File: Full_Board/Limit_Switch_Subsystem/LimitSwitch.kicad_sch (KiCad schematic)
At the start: 6 parts, among them J8 OQ0212500000G

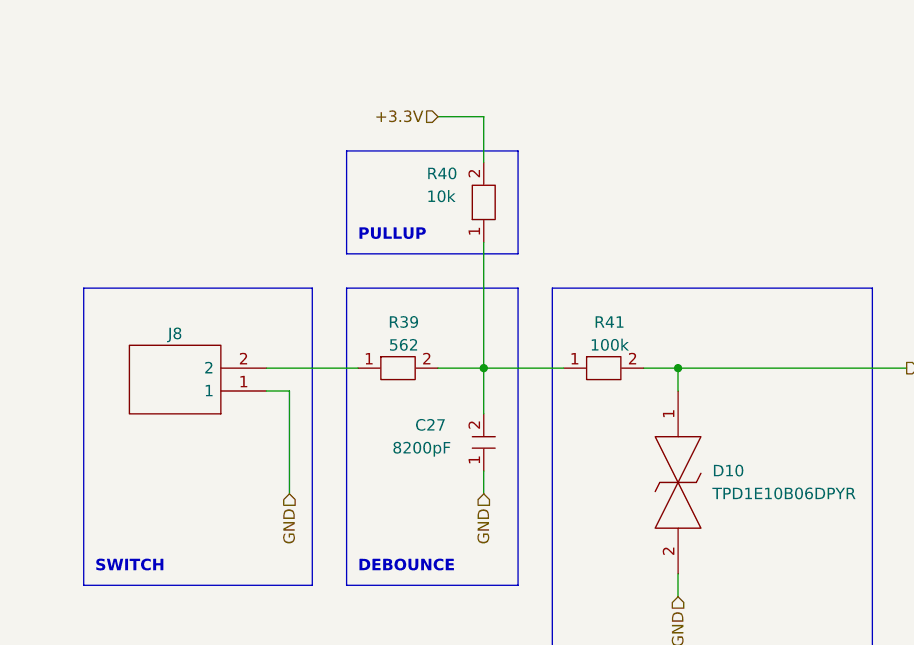
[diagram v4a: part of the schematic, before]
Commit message: Added a fuse and fixed ERC
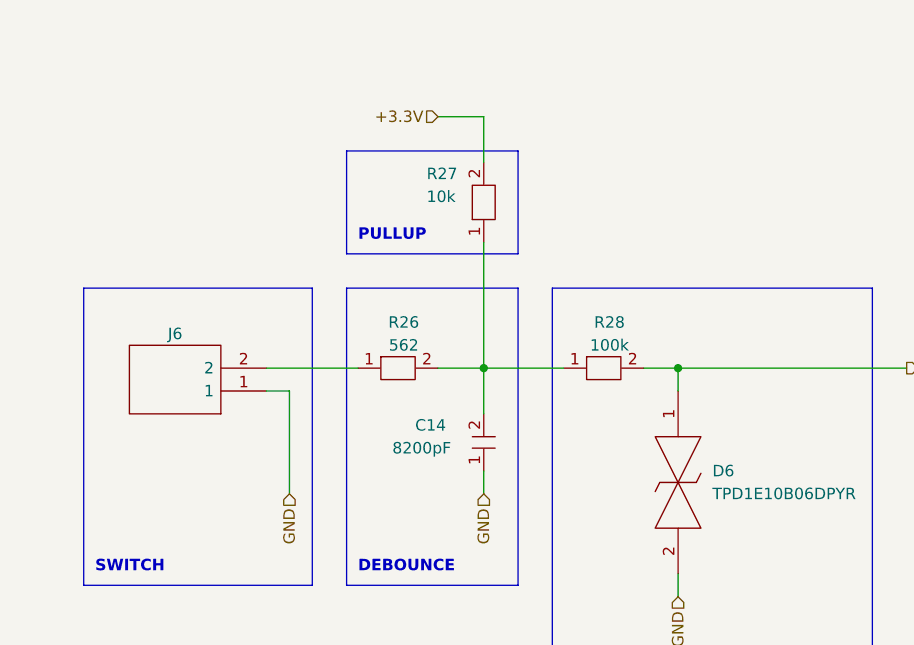
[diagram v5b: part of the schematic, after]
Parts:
- renumbered C27 to C14, D10 to D6, J8 to J6, R39 to R26, R40 to R27, R41 to R28
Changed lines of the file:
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@@
+    (stroke (width 0) (type default) (color 0 0 0 0))
+  )
+  (wire (pts (xy 143.51 62.23) (xy 143.51 67.31))
     (stroke (width 0) (type default) (color 0 0 0 0))
   )
   (wire (pts (xy 165.1 90.17) (xy 190.5 90.17))
-    (stroke (width 0) (type default) (color 0 0 0 0))
-  )
-  (wire (pts (xy 143.51 62.23) (xy 143.51 67.31))
     (stroke (width 0) (type default) (color 0 0 0 0))
   )
@@
     (effects (font (size 1.27 1.27)) (justify right))
   )
-  (symbol (lib_id "OQ0212500000G:OQ0212500000G") (at 119.38 92.71 180) (unit 1)
-    (in_bom yes) (on_board yes)
-    (property "Reference" "J8" (id 0) (at 109.22 86.36 0))
+  (symbol (lib_id "OQ0212500000G:OQ0212500000G") (at 119.38 92.71 180)
+    (in_bom yes) (on_board yes)
+    (property "Reference" "J6" (id 0) (at 109.22 86.36 0))
     (property "Value" "OQ0212500000G" (id 1) (at 109.22 85.09 0)
       (effects (font (size 1.27 1.27)) hide)
@@
     (pin "2")
   )
-  (symbol (lib_id "CR0402-FX-5620GLF:CR0402-FX-5620GLF") (at 129.54 90.17 0) (unit 1)
-    (in_bom yes) (on_board yes)
-    (property "Reference" "R39" (id 0) (at 134.62 85.09 0))
+  (symbol (lib_id "CR0402-FX-5620GLF:CR0402-FX-5620GLF") (at 129.54 90.17 0)
+    (in_bom yes) (on_board yes)
+    (property "Reference" "R26" (id 0) (at 134.62 85.09 0))
     (property "Value" "562" (id 1) (at 134.62 87.63 0))
     (property "Footprint" "CR0402-FX-5620GLF:RESC1005X40N" (id 2) (at 143.51 88.9 0)
@@
     (pin "2")
   )
-  (symbol (lib_id "RMCF1206FT10K0:10k") (at 143.51 76.2 90) (unit 1)
-    (in_bom yes) (on_board yes)
-    (property "Reference" "R40" (id 0) (at 137.16 68.58 90)
+  (symbol (lib_id "RMCF1206FT10K0:10k") (at 143.51 76.2 90)
+    (in_bom yes) (on_board yes)
+    (property "Reference" "R27" (id 0) (at 137.16 68.58 90)
       (effects (font (size 1.27 1.27)) (justify right))
     )
@@
     (pin "2")
   )
-  (symbol (lib_id "RCV2512100KFKEGAT:RCV2512100KFKEGAT") (at 152.4 90.17 0) (unit 1)
-    (in_bom yes) (on_board yes)
-    (property "Reference" "R41" (id 0) (at 157.48 85.09 0))
+  (symbol (lib_id "RCV2512100KFKEGAT:RCV2512100KFKEGAT") (at 152.4 90.17 0)
+    (in_bom yes) (on_board yes)
+    (property "Reference" "R28" (id 0) (at 157.48 85.09 0))
     (property "Value" "100k" (id 1) (at 157.48 87.63 0))
     (property "Footprint" "RCV2512100KFKEGAT:RESC6332X70N" (id 2) (at 166.37 88.9 0)
@@
     (pin "2")
   )
-  (symbol (lib_id "C1210C822K2RACAUTO:C1210C822K2RACAUTO") (at 143.51 101.6 90) (unit 1)
-    (in_bom yes) (on_board yes)
-    (property "Reference" "C27" (id 0) (at 135.89 96.52 90)
+  (symbol (lib_id "C1210C822K2RACAUTO:C1210C822K2RACAUTO") (at 143.51 101.6 90)
+    (in_bom yes) (on_board yes)
+    (property "Reference" "C14" (id 0) (at 135.89 96.52 90)
       (effects (font (size 1.27 1.27)) (justify right))
     )
@@
     (pin "2")
   )
-  (symbol (lib_id "TPD1E10B06DPYR:TPD1E10B06DPYR") (at 165.1 92.71 270) (unit 1)
-    (in_bom yes) (on_board yes)
-    (property "Reference" "D10" (id 0) (at 168.91 101.6 90)
+  (symbol (lib_id "TPD1E10B06DPYR:TPD1E10B06DPYR") (at 165.1 92.71 270)
+    (in_bom yes) (on_board yes)
+    (property "Reference" "D6" (id 0) (at 168.91 101.6 90)
       (effects (font (size 1.27 1.27)) (justify left))
     )

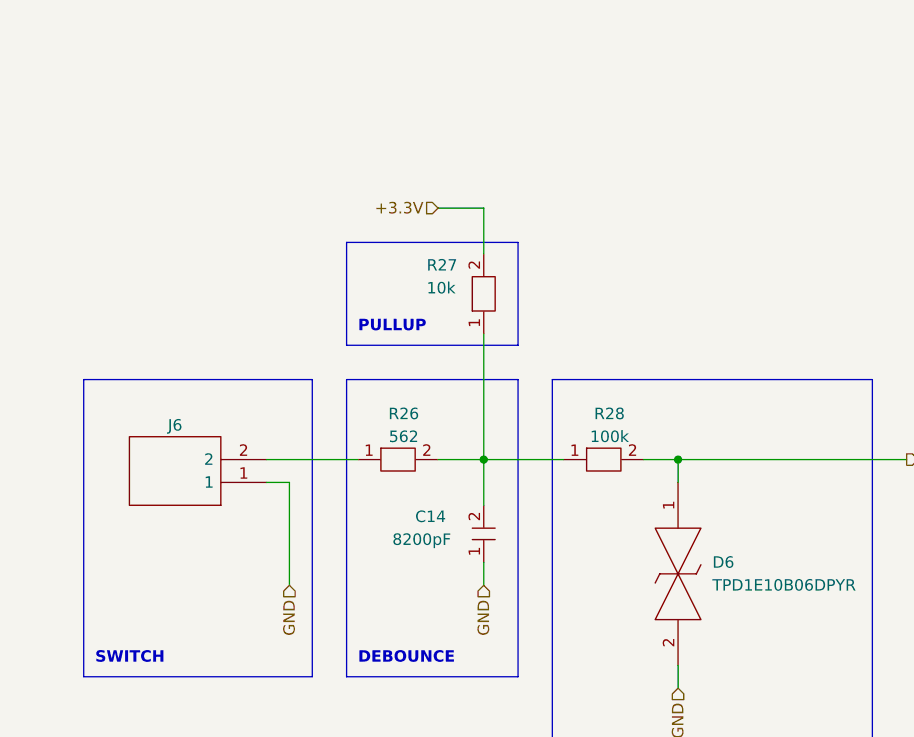
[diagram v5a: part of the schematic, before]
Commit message: Redo sensor network, redo MSP432 connections, redo LED subsystem, add shunts throughout, ERC still passes
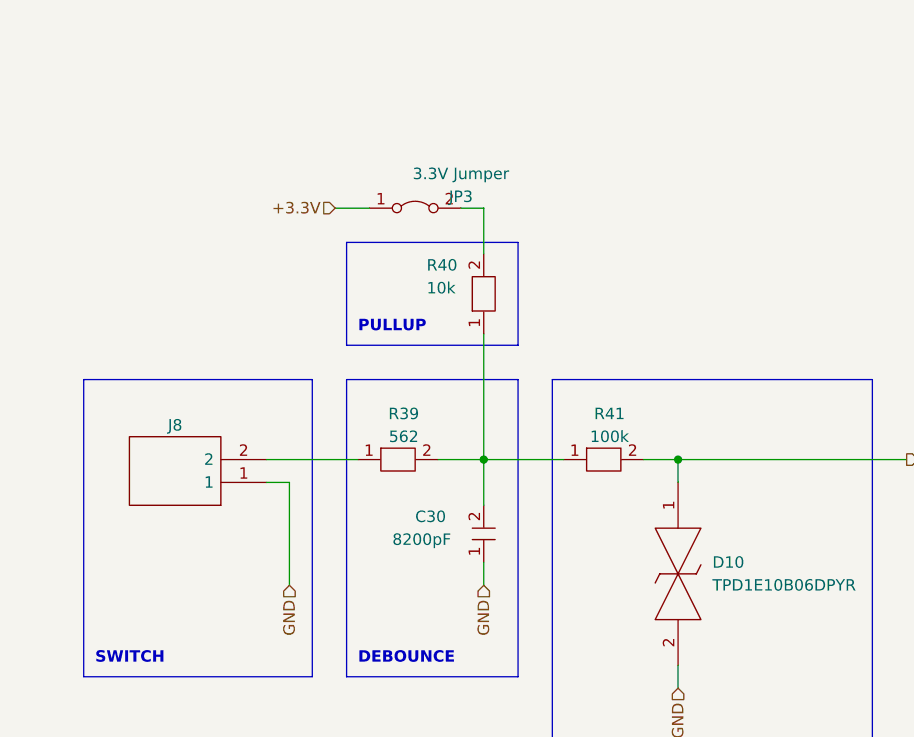
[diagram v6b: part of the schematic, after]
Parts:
- added JP3: 3.3V Jumper, TestPoint:TestPoint_2Pads_Pitch2.54mm_Drill0.8mm, symbol Jumper:Jumper_2_Bridged
- renumbered C14 to C30, D6 to D10, J6 to J8, R26 to R39, R27 to R40, R28 to R41
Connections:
- net +3.3V: now also JP3.1 (A); no longer R40.2
- new net: JP3.2 (B), R40.2
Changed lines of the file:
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@@
     (stroke (width 0) (type default) (color 0 0 0 0))
   )
-  (wire (pts (xy 138.43 62.23) (xy 143.51 62.23))
+  (wire (pts (xy 127 62.23) (xy 130.81 62.23))
     (stroke (width 0) (type default) (color 0 0 0 0))
   )
@@
   )
   (polyline (pts (xy 128.27 81.28) (xy 147.32 81.28))
+    (stroke (width 0) (type default) (color 0 0 0 0))
+  )
+  (wire (pts (xy 140.97 62.23) (xy 143.51 62.23))
     (stroke (width 0) (type default) (color 0 0 0 0))
   )
@@
     (effects (font (size 1.27 1.27) (thickness 0.254) bold) (justify left bottom))
   )
-  (hierarchical_label "+3.3V" (shape input) (at 138.43 62.23 180)
+  (hierarchical_label "+3.3V" (shape input) (at 127 62.23 180)
     (effects (font (size 1.27 1.27)) (justify right))
   )
@@
     (effects (font (size 1.27 1.27)) (justify right))
   )
-  (symbol (lib_id "OQ0212500000G:OQ0212500000G") (at 119.38 92.71 180)
-    (in_bom yes) (on_board yes)
-    (property "Reference" "J6" (id 0) (at 109.22 86.36 0))
+  (symbol (lib_id "OQ0212500000G:OQ0212500000G") (at 119.38 92.71 180) (unit 1)
+    (in_bom yes) (on_board yes)
+    (property "Reference" "J8" (id 0) (at 109.22 86.36 0))
     (property "Value" "OQ0212500000G" (id 1) (at 109.22 85.09 0)
       (effects (font (size 1.27 1.27)) hide)
@@
     (pin "2")
   )
-  (symbol (lib_id "CR0402-FX-5620GLF:CR0402-FX-5620GLF") (at 129.54 90.17 0)
-    (in_bom yes) (on_board yes)
-    (property "Reference" "R26" (id 0) (at 134.62 85.09 0))
+  (symbol (lib_id "CR0402-FX-5620GLF:CR0402-FX-5620GLF") (at 129.54 90.17 0) (unit 1)
+    (in_bom yes) (on_board yes)
+    (property "Reference" "R39" (id 0) (at 134.62 85.09 0))
     (property "Value" "562" (id 1) (at 134.62 87.63 0))
     (property "Footprint" "CR0402-FX-5620GLF:RESC1005X40N" (id 2) (at 143.51 88.9 0)
@@
     (pin "2")
   )
-  (symbol (lib_id "RMCF1206FT10K0:10k") (at 143.51 76.2 90)
-    (in_bom yes) (on_board yes)
-    (property "Reference" "R27" (id 0) (at 137.16 68.58 90)
+  (symbol (lib_id "RMCF1206FT10K0:10k") (at 143.51 76.2 90) (unit 1)
+    (in_bom yes) (on_board yes)
+    (property "Reference" "R40" (id 0) (at 137.16 68.58 90)
       (effects (font (size 1.27 1.27)) (justify right))
     )
@@
     (pin "2")
   )
-  (symbol (lib_id "RCV2512100KFKEGAT:RCV2512100KFKEGAT") (at 152.4 90.17 0)
-    (in_bom yes) (on_board yes)
-    (property "Reference" "R28" (id 0) (at 157.48 85.09 0))
+  (symbol (lib_id "RCV2512100KFKEGAT:RCV2512100KFKEGAT") (at 152.4 90.17 0) (unit 1)
+    (in_bom yes) (on_board yes)
+    (property "Reference" "R41" (id 0) (at 157.48 85.09 0))
     (property "Value" "100k" (id 1) (at 157.48 87.63 0))
     (property "Footprint" "RCV2512100KFKEGAT:RESC6332X70N" (id 2) (at 166.37 88.9 0)
@@
     (pin "2")
   )
-  (symbol (lib_id "C1210C822K2RACAUTO:C1210C822K2RACAUTO") (at 143.51 101.6 90)
-    (in_bom yes) (on_board yes)
-    (property "Reference" "C14" (id 0) (at 135.89 96.52 90)
+  (symbol (lib_id "C1210C822K2RACAUTO:C1210C822K2RACAUTO") (at 143.51 101.6 90) (unit 1)
+    (in_bom yes) (on_board yes)
+    (property "Reference" "C30" (id 0) (at 135.89 96.52 90)
       (effects (font (size 1.27 1.27)) (justify right))
     )
@@
     (pin "2")
   )
-  (symbol (lib_id "TPD1E10B06DPYR:TPD1E10B06DPYR") (at 165.1 92.71 270)
-    (in_bom yes) (on_board yes)
-    (property "Reference" "D6" (id 0) (at 168.91 101.6 90)
+  (symbol (lib_id "Jumper:Jumper_2_Bridged") (at 135.89 62.23 0) (unit 1)
+    (in_bom yes) (on_board yes)
+    (property "Reference" "JP3" (id 0) (at 140.97 60.96 0))
+    (property "Value" "3.3V Jumper" (id 1) (at 140.97 58.42 0))
+    (property "Footprint" "TestPoint:TestPoint_2Pads_Pitch2.54mm_Drill0.8mm" (id 2) (at 135.89 62.23 0)
+      (effects (font (size 1.27 1.27)) hide)
+    )
+    (property "Datasheet" "~" (id 3) (at 135.89 62.23 0)
+      (effects (font (size 1.27 1.27)) hide)
+    )
+    (property "Manufacturers Part Number" "PH1-02-UA" (id 4) (at 135.89 62.23 0)
+      (effects (font (size 1.27 1.27)) hide)
+    )
+    (property "Digikey Part Number" "2057-PH1-02-UA-ND" (id 5) (at 135.89 62.23 0)
+      (effects (font (size 1.27 1.27)) hide)
+    )
+    (property "Mouser Part Number" "" (id 6) (at 135.89 62.23 0)
+      (effects (font (size 1.27 1.27)) hide)
+    )
+    (property "Digikey Link" "https://www.digikey.com/en/products/detail/adam-tech/PH1-02-UA/9830266" (id 7) (at 135.89 62.23 0)
+      (effects (font (size 1.27 1.27)) hide)
+    )
+    (property "Mouser Link" "" (id 8) (at 135.89 62.23 0)
+      (effects (font (size 1.27 1.27)) hide)
+    )
+    (pin "1")
+    (pin "2")
+  )
+  (symbol (lib_id "TPD1E10B06DPYR:TPD1E10B06DPYR") (at 165.1 92.71 270) (unit 1)
+    (in_bom yes) (on_board yes)
+    (property "Reference" "D10" (id 0) (at 168.91 101.6 90)
       (effects (font (size 1.27 1.27)) (justify left))
     )

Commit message: Added LEDs to the power supply
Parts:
- renumbered JP3 to JP11
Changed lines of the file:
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@@
   (symbol (lib_id "Jumper:Jumper_2_Bridged") (at 135.89 62.23 0) (unit 1)
     (in_bom yes) (on_board yes)
-    (property "Reference" "JP3" (id 0) (at 140.97 60.96 0))
+    (property "Reference" "JP11" (id 0) (at 140.97 60.96 0))
     (property "Value" "3.3V Jumper" (id 1) (at 140.97 58.42 0))
     (property "Footprint" "TestPoint:TestPoint_2Pads_Pitch2.54mm_Drill0.8mm" (id 2) (at 135.89 62.23 0)

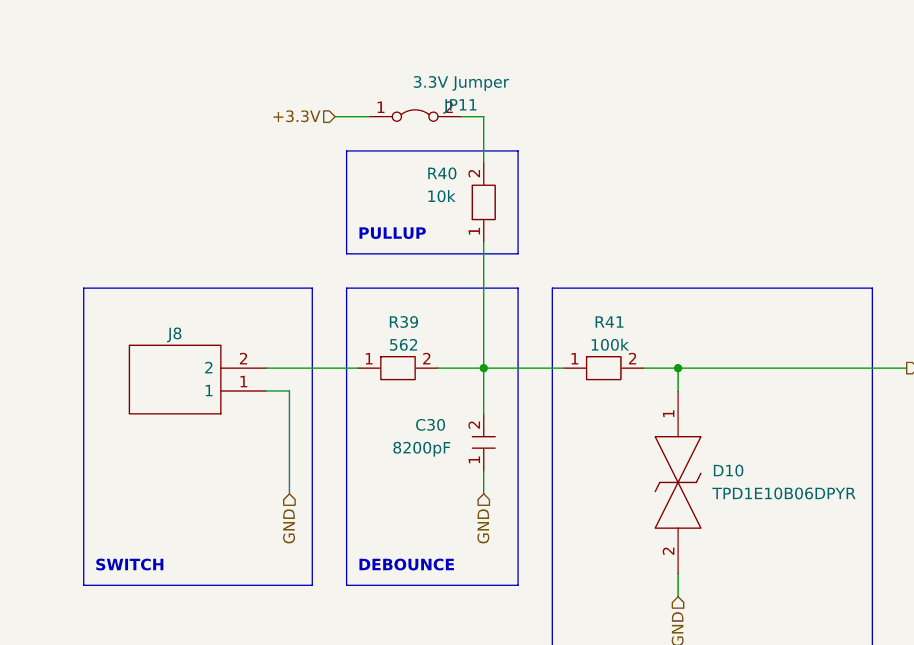
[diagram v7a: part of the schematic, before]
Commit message: Resolve misconfigured components, replace PCB from now completed schematic
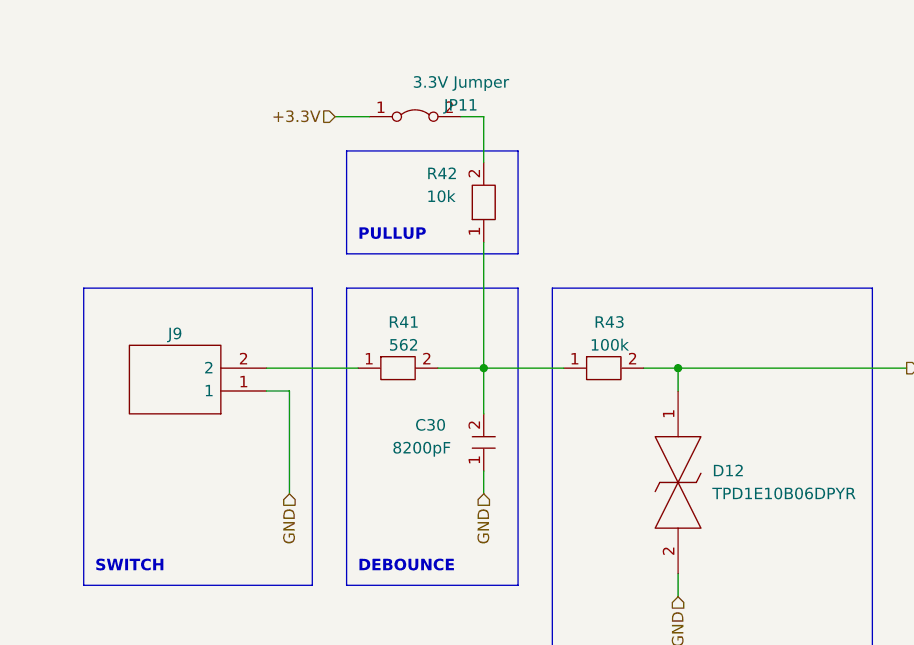
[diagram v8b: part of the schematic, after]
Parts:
- R42: renamed from R40; footprint RESC3225X74N -> RMCF1206FT10K0:RMCF1206FT10K0; Digikey link https://www.digikey.com/en/products/detail/stackpole-electronics-inc/RMCF1206FT10K0/1759669?s=N4IgTCBcDaIEoFkDCAxAjGADANhQFTUwGlMQBdAXyA -> https://www.digikey.com/en/products/detail/stackpole-electronics-inc/RMCF1206FT10K0/1759669
- renumbered D10 to D12, J8 to J9, R39 to R41, R41 to R43
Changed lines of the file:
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@@
   (symbol (lib_id "OQ0212500000G:OQ0212500000G") (at 119.38 92.71 180) (unit 1)
     (in_bom yes) (on_board yes)
-    (property "Reference" "J8" (id 0) (at 109.22 86.36 0))
+    (property "Reference" "J9" (id 0) (at 109.22 86.36 0))
     (property "Value" "OQ0212500000G" (id 1) (at 109.22 85.09 0)
       (effects (font (size 1.27 1.27)) hide)
@@
   (symbol (lib_id "CR0402-FX-5620GLF:CR0402-FX-5620GLF") (at 129.54 90.17 0) (unit 1)
     (in_bom yes) (on_board yes)
-    (property "Reference" "R39" (id 0) (at 134.62 85.09 0))
+    (property "Reference" "R41" (id 0) (at 134.62 85.09 0))
     (property "Value" "562" (id 1) (at 134.62 87.63 0))
     (property "Footprint" "CR0402-FX-5620GLF:RESC1005X40N" (id 2) (at 143.51 88.9 0)
@@
   (symbol (lib_id "RMCF1206FT10K0:10k") (at 143.51 76.2 90) (unit 1)
     (in_bom yes) (on_board yes)
-    (property "Reference" "R40" (id 0) (at 137.16 68.58 90)
+    (property "Reference" "R42" (id 0) (at 137.16 68.58 90)
       (effects (font (size 1.27 1.27)) (justify right))
     )
@@
       (effects (font (size 1.27 1.27)) (justify right))
     )
-    (property "Footprint" "RESC3225X74N" (id 2) (at 142.24 62.23 0)
-      (effects (font (size 1.27 1.27)) (justify left) hide)
-    )
-    (property "Datasheet" "https://www.vishay.com/docs/68043/crma.pdf" (id 3) (at 144.78 62.23 0)
+    (property "Footprint" "RMCF1206FT10K0:RMCF1206FT10K0" (id 2) (at 142.24 62.23 0)
+      (effects (font (size 1.27 1.27)) (justify left) hide)
+    )
+    (property "Datasheet" "https://www.seielect.com/catalog/sei-rmcf_rmcp.pdf" (id 3) (at 144.78 62.23 0)
       (effects (font (size 1.27 1.27)) (justify left) hide)
     )
@@
       (effects (font (size 1.27 1.27)) (justify left) hide)
     )
-    (property "Digikey link" "https://www.digikey.com/en/products/detail/stackpole-electronics-inc/RMCF1206FT10K0/1759669?s=N4IgTCBcDaIEoFkDCAxAjGADANhQFTUwGlMQBdAXyA" (id 7) (at 154.94 62.23 0)
+    (property "Digikey link" "https://www.digikey.com/en/products/detail/stackpole-electronics-inc/RMCF1206FT10K0/1759669" (id 7) (at 154.94 62.23 0)
       (effects (font (size 1.27 1.27)) (justify left) hide)
     )
@@
   (symbol (lib_id "RCV2512100KFKEGAT:RCV2512100KFKEGAT") (at 152.4 90.17 0) (unit 1)
     (in_bom yes) (on_board yes)
-    (property "Reference" "R41" (id 0) (at 157.48 85.09 0))
+    (property "Reference" "R43" (id 0) (at 157.48 85.09 0))
     (property "Value" "100k" (id 1) (at 157.48 87.63 0))
     (property "Footprint" "RCV2512100KFKEGAT:RESC6332X70N" (id 2) (at 166.37 88.9 0)
@@
   (symbol (lib_id "TPD1E10B06DPYR:TPD1E10B06DPYR") (at 165.1 92.71 270) (unit 1)
     (in_bom yes) (on_board yes)
-    (property "Reference" "D10" (id 0) (at 168.91 101.6 90)
+    (property "Reference" "D12" (id 0) (at 168.91 101.6 90)
       (effects (font (size 1.27 1.27)) (justify left))
     )
